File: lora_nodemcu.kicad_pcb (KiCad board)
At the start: 4 copper layers, 26 x 43.5 mm, 10 parts, among them U1 RFM95, U2 LM1117-3.3, U3 WeMos_mini

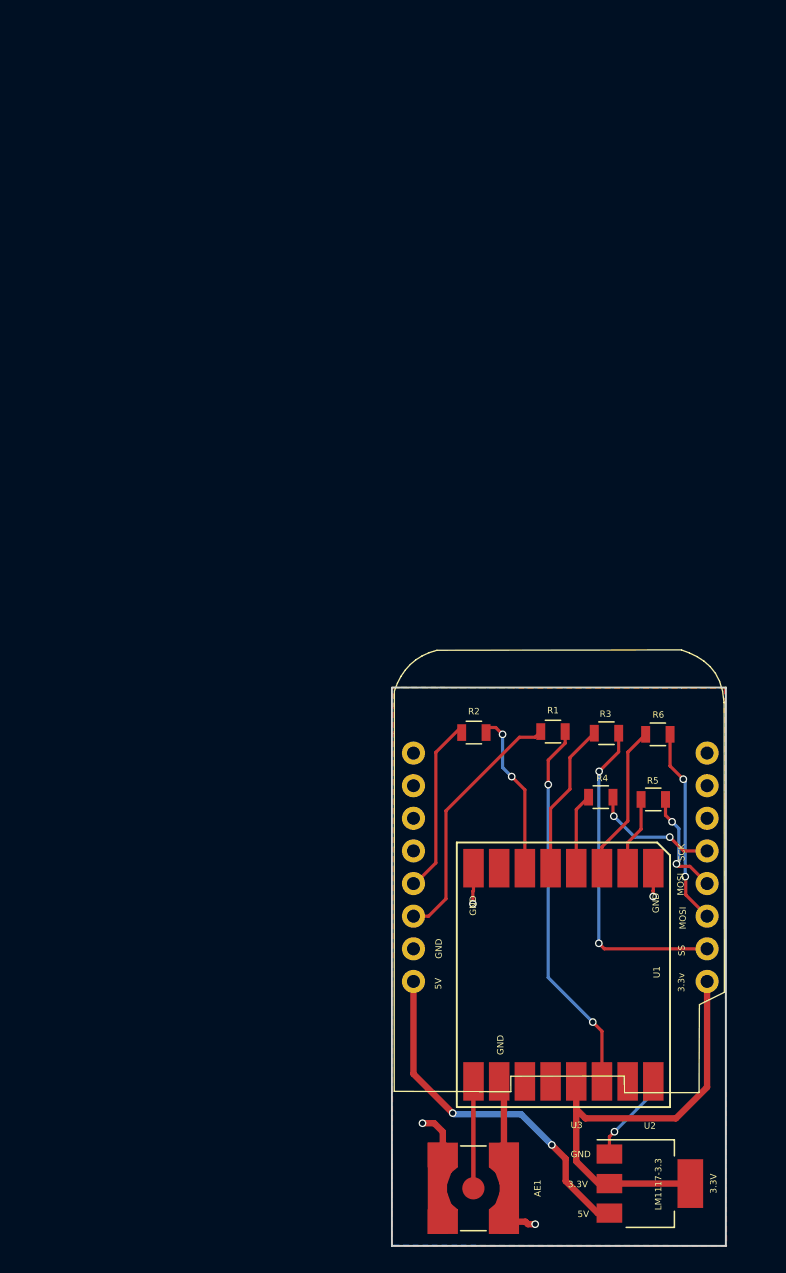
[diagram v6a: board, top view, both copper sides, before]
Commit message: Missing caps need to be added to voltage regulator.  Making a save to repo before pushing to Sudomesh repo.
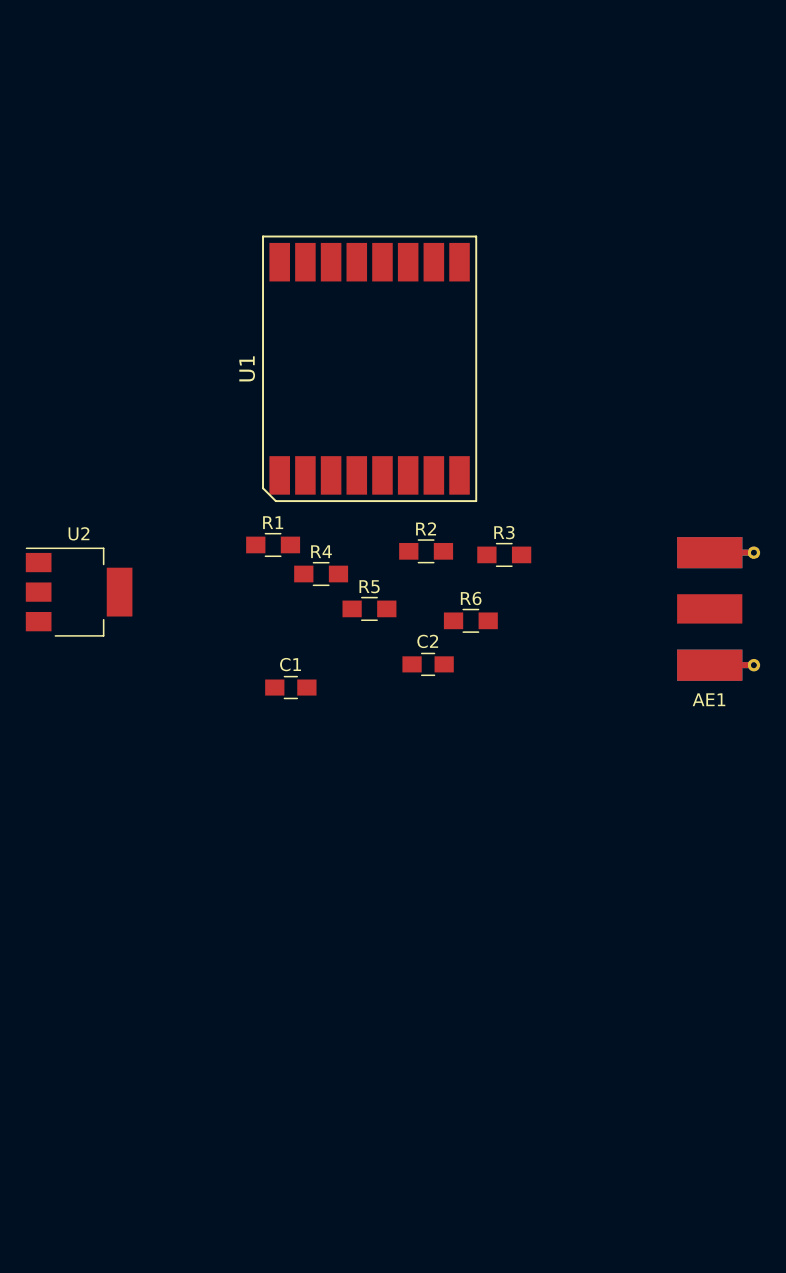
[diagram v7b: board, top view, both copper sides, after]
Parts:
- removed U3: WeMos_mini, DisasterRadio:D1_mini_Hat
- added C1: 10u, Capacitors_SMD:C_0805_HandSoldering, F.Cu at (142.4, 111.1)
- added C2: 10u, Capacitors_SMD:C_0805_HandSoldering, F.Cu at (153.1, 109.3)
- AE1: value Antenna -> Antenna_Shield; footprint Connectors:SMA_SMD_Jack_Straight -> Connectors_Molex:Molex_SMA_Jack_Edge_Mount
- R1, R2, R3, R4, R5, R6: footprint Resistors_SMD:R_0805 -> Resistors_SMD:R_0805_HandSoldering
- moved U2 64.0 mm to (125.9, 103.7)
- moved U1 49.5 mm to (148.5, 86.3), turned to 0 degrees
- moved AE1 49.4 mm to (176.7, 105.0), turned to 0 degrees
- moved R4 27.9 mm to (144.7, 102.3), turned to 0 degrees
- moved R5 26.6 mm to (148.5, 105.0), turned to 0 degrees
- moved R1 26.2 mm to (141.0, 100.0)
- moved R6 17.0 mm to (156.4, 105.9), turned to 0 degrees
- moved R3 16.0 mm to (159.0, 100.8), turned to 0 degrees
- moved R2 14.6 mm to (152.9, 100.5)
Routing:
- net +3V3: track 37.7 -> 0.00 mm
- net GND: track 30.9 -> 0.00 mm, vias 5 -> 0
- net Net-(R1-Pad2): track 29.6 -> 0.00 mm, vias 2 -> 0
- net +5V: track 28.0 -> 0.00 mm, vias 2 -> 0
- net /SS: track 25.7 -> 0.00 mm, vias 2 -> 0
- net Net-(R1-Pad1): track 19.9 -> 0.00 mm
- net /MOSI: track 15.4 -> 0.00 mm, vias 2 -> 0
- net Net-(R2-Pad1): track 13.8 -> 0.00 mm
- net Net-(R2-Pad2): track 12.7 -> 0.00 mm, vias 2 -> 0
- net Net-(R3-Pad2): track 11.9 -> 0.00 mm
- net Net-(R6-Pad2): track 11.8 -> 0.00 mm
- net /SCK: track 9.89 -> 0.00 mm, vias 2 -> 0
- net /MISO: track 8.55 -> 0.00 mm, vias 2 -> 0
- net Net-(AE1-Pad1): track 8.33 -> 0.00 mm
- net Net-(R4-Pad2): track 5.93 -> 0.00 mm
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- removed copper zone on In2.Cu, net +3V3
- removed copper zone on B.Cu, net GND
- removed copper zone on F.Cu, net GND
- removed copper zone on In1.Cu, net GND
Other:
- board outline removed
- board text removed: "3.3V"
- board text removed: "3.3v"
- board text removed: "5V"
- board text removed: "GND"
- board text removed: "LM1117-3.3"
- board text removed: "MOSI"
- board text removed: "SCK"
- board text removed: "SS"

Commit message: Saving changes to circuit board prior to reworking yet again.
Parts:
- added U3: WeMos_mini, DisasterRadio:D1_mini_board, F.Cu at (148.7, 87.1)
- C1, C2, R1, R2, R3, R4, R5, R6: moved to B.Cu
- moved AE1 34.8 mm to (142.0, 103.3), turned to 90 degrees
- moved U2 29.1 mm to (155.0, 104.0)
- moved R4 22.4 mm to (154.4, 82.1), turned to 180 degrees
- moved R2 19.7 mm to (146.2, 82.0)
- moved R5 19.1 mm to (154.4, 86.8), turned to 180 degrees
- moved R6 18.9 mm to (146.5, 89.8), turned to 180 degrees
- moved R1 15.1 mm to (146.3, 85.9)
- moved C1 12.4 mm to (144.3, 98.9), turned to 180 degrees
- moved C2 11.4 mm to (158.2, 99.1)
- moved R3 11.1 mm to (154.4, 90.7), turned to 180 degrees
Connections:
- net Net-(AE1-Pad1) renamed /50Ohm
- U1 pad 10: GND -> Net-(U1-Pad10)
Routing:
- net +5V: track 0.00 -> 21.8 mm, vias 0 -> 2
- net Net-(R2-Pad2): track 0.00 -> 18.0 mm, vias 0 -> 2
- net Net-(R5-Pad2): track 0.00 -> 16.3 mm, vias 0 -> 2
- net Net-(R4-Pad2): track 0.00 -> 14.9 mm, vias 0 -> 2
- net GND: track 0.00 -> 13.7 mm, vias 0 -> 3
- net /MOSI: track 0.00 -> 13.0 mm, vias 0 -> 2
- net +3V3: track 0.00 -> 11.5 mm, vias 0 -> 4
- net Net-(R1-Pad2): track 0.00 -> 8.84 mm, vias 0 -> 1
- net Net-(R1-Pad1): track 0.00 -> 8.35 mm, vias 0 -> 2
- net Net-(R2-Pad1): track 0.00 -> 7.64 mm, vias 0 -> 2
- net Net-(R3-Pad2): track 0.00 -> 6.55 mm, vias 0 -> 2
- net /SCK: track 0.00 -> 5.83 mm, vias 0 -> 1
- net /SS: track 0.00 -> 4.93 mm, vias 0 -> 2
- net Net-(R6-Pad2): track 0.00 -> 4.91 mm, vias 0 -> 1
- net /MISO: track 0.00 -> 4.52 mm, vias 0 -> 2
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- added copper zone on In2.Cu, net +3V3
- added copper zone on B.Cu, net GND
- added copper zone on F.Cu, net GND
- added copper zone on In1.Cu, net GND
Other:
- board outline added: 25.8 x 32.9 mm
- net class power added: clearance 0.2, trace_width 0.5, via_dia 0.8, via_drill 0.5
